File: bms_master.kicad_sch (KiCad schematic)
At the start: 94 parts, among them J1 Conn_01x02, J2 Conn_01x02, J3 Conn_01x02, J4 Conn_01x04, J5 Conn_01x04, J6 Conn_01x06, Q1 PMV15ENE, Q2 PMV74EPE, Q3 PMV74EPE, SW1 SW_Push, U1 TPS25961, U10 MAX6126, U2 TPS7B88, U3 MCP1700x-330xxMB, U4 STM32F103C8Tx, U5 TPS3851, U6 SN65HVD1050D, U7 M24C64-R, U8 741G3157, U9 MAX11163, Y1 8M

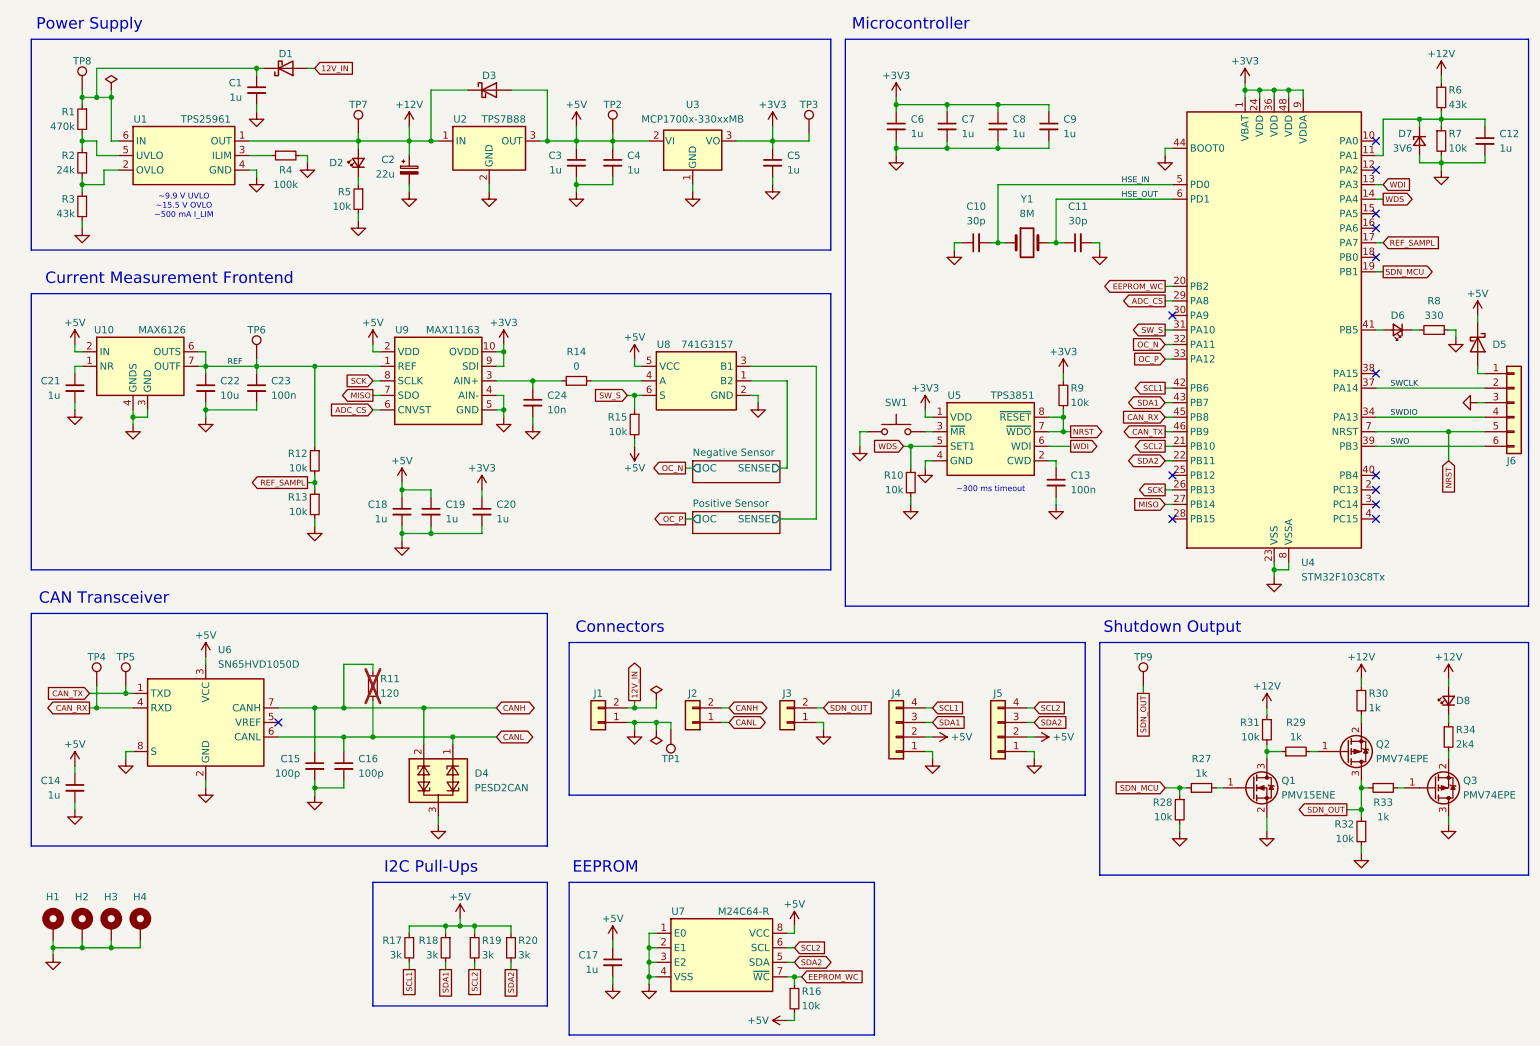
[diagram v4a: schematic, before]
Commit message: *: Switch from the TPS25961 eFuse to the TPS26625
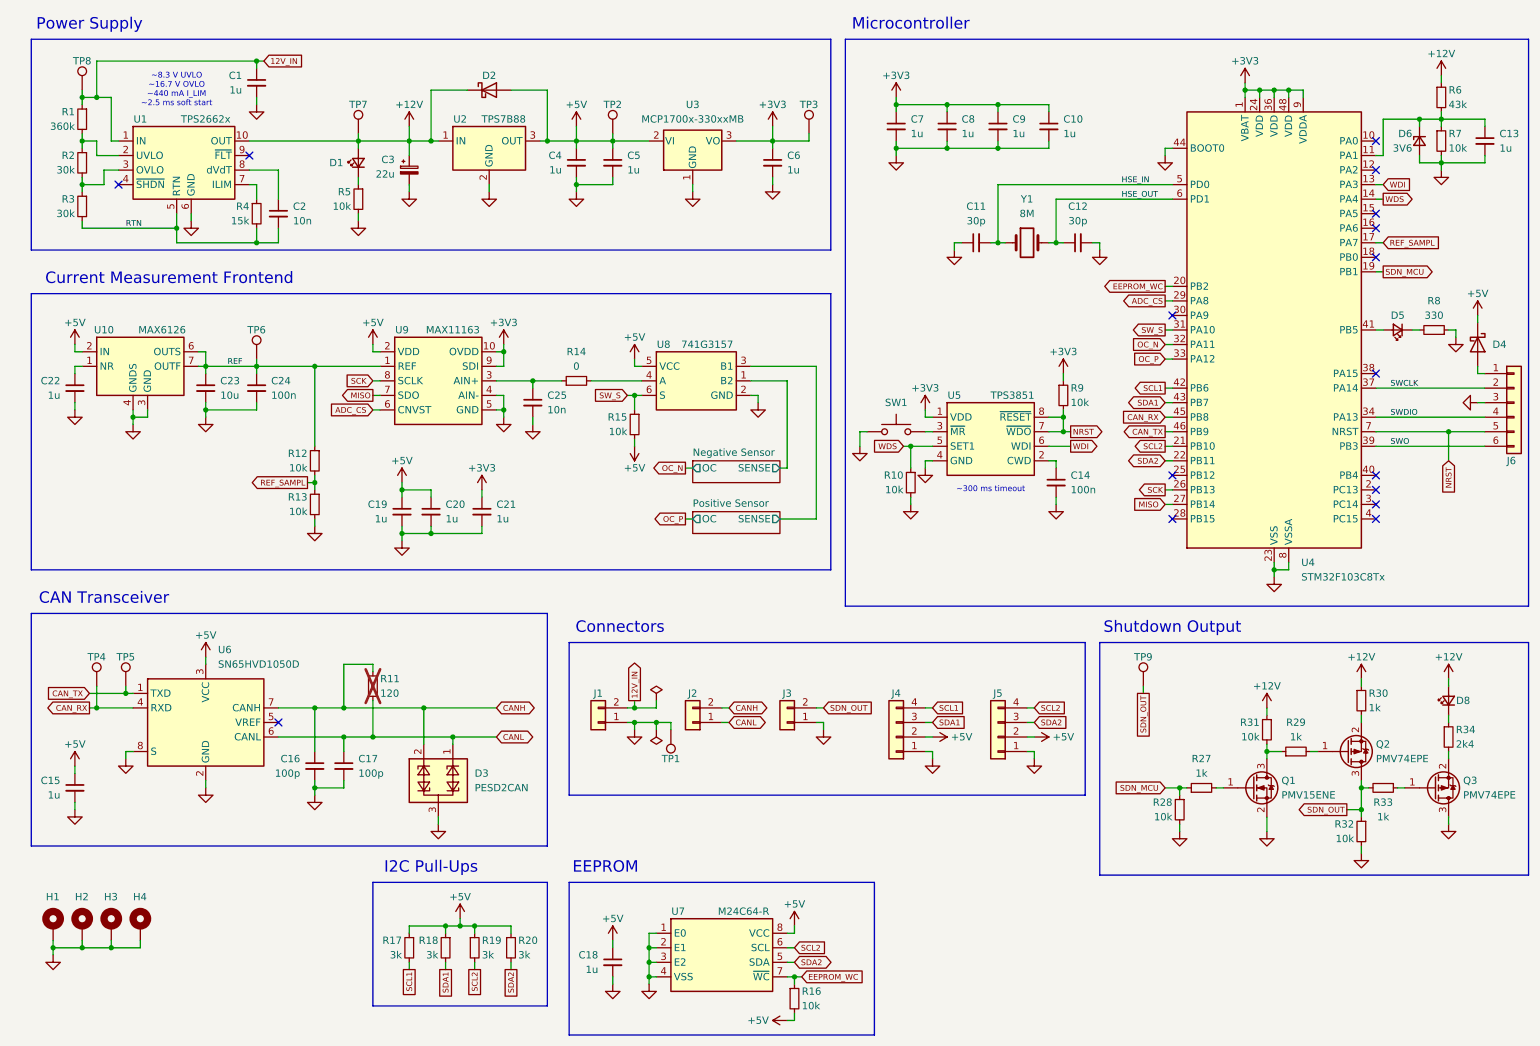
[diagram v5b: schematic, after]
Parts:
- removed D1: D_Schottky, Diode_SMD:D_SOD-323, symbol Device:D_Schottky
- removed U1: TPS25961, Package_SON:WSON-6-1EP_2x2mm_P0.65mm_EP1x1.6mm, symbol yfs:TPS25961
- added C2: 10n, Capacitor_SMD:C_0603_1608Metric, symbol Device:C_Small
- added U1: TPS2662x, Package_SON:VSON-10-1EP_3x3mm_P0.5mm_EP1.65x2.4mm, symbol yfs:TPS2662x
- R1: value 470k -> 360k
- R2: value 24k -> 30k
- R3: value 43k -> 30k
- R4: value 100k -> 15k
- renumbered C9 to C10, C10 to C11, C11 to C12, C12 to C13, C13 to C14, C14 to C15, C15 to C16, C16 to C17, C17 to C18, C18 to C19, C19 to C20, C20 to C21, C21 to C22, C22 to C23, C23 to C24, C24 to C25, C2 to C3, C3 to C4, C4 to C5, C5 to C6, C6 to C7, C7 to C8, C8 to C9, D2 to D1, D3 to D2, D4 to D3, D5 to D4, D6 to D5, D7 to D6
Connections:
- net +12V: now also U1.10 (OUT)
- net 12V_IN: now also C1.1, R1.1, TP8.1, U1.1 (IN)
- net GND: now also U1.6 (GND); no longer R3.2, R4.2
- net at R1.2, R2.1: now also U1.2 (UVLO)
- net at R2.2, R3.1: now also U1.3 (OVLO)
- net at R4.1: now also U1.7 (ILIM)
- new net: C2.1, U1.8 (dVdT)
- new net RTN: C2.2, R3.2, R4.2, U1.11 (RTN), U1.5 (RTN)
- no-connect marks 14 -> 16
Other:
- note added: "~8.3 V UVLO ~16.7 V OVLO ~440 mA I_LIM ~2.5 ms soft start"
- note removed: "~9.9 V UVLO ~15.5 V OVLO ~500 mA I_LIM"
- moved on the sheet: C1

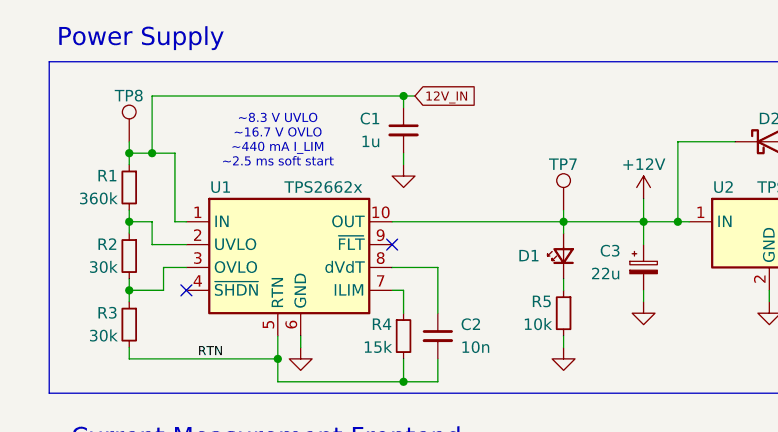
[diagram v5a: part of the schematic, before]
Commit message: *: Add a TVS diode on the LVS input
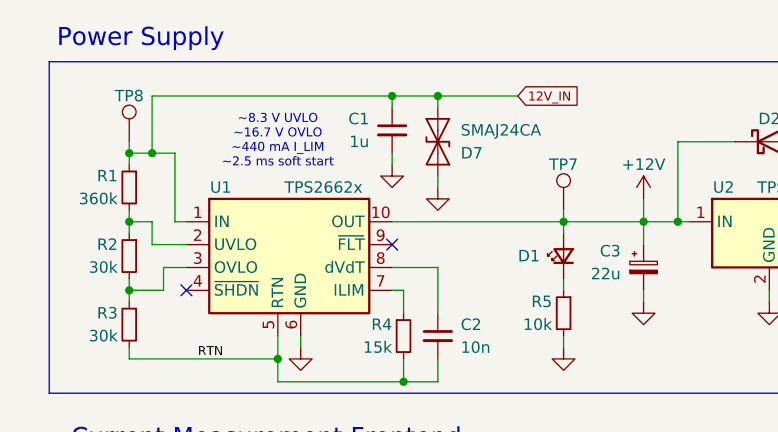
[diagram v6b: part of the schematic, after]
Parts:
- added D7: SMAJ24CA, Diode_SMD:D_SMA, symbol Diode:SMAJ24CA
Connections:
- net 12V_IN: now also D7.2 (A2)
- net GND: now also D7.1 (A1)
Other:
- moved on the sheet: C1
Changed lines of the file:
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@@
 	)
 	(junction
+		(at 58.42 21.59)
+		(diameter 0)
+		(color 0 0 0 0)
+	)
+	(junction
 		(at 128.27 176.53)
 		(diameter 0)
@@
 	)
 	(junction
+		(at 63.5 21.59)
+		(diameter 0)
+		(color 0 0 0 0)
+	)
+	(junction
 		(at 237.49 110.49)
 		(diameter 0)
@@
 	)
 	(junction
-		(at 59.69 21.59)
-		(diameter 0)
-		(color 0 0 0 0)
-	)
-	(junction
 		(at 220.98 148.59)
 		(diameter 0)
@@
 	(wire
 		(pts
-			(xy 59.69 29.21) (xy 59.69 27.94)
+			(xy 58.42 29.21) (xy 58.42 27.94)
 		)
 		(stroke
@@
 	(wire
 		(pts
+			(xy 63.5 21.59) (xy 72.39 21.59)
+		)
+		(stroke
+			(width 0)
+			(type default)
+		)
+	)
+	(wire
+		(pts
 			(xy 267.97 86.36) (xy 274.32 86.36)
 		)
@@
 	(wire
 		(pts
-			(xy 60.96 21.59) (xy 59.69 21.59)
-		)
-		(stroke
-			(width 0)
-			(type default)
-		)
-	)
-	(wire
-		(pts
 			(xy 262.89 38.1) (xy 262.89 39.37)
 		)
@@
 	(wire
 		(pts
+			(xy 63.5 30.48) (xy 63.5 31.75)
+		)
+		(stroke
+			(width 0)
+			(type default)
+		)
+	)
+	(wire
+		(pts
 			(xy 31.75 134.62) (xy 38.1 134.62)
 		)
@@
 	(wire
 		(pts
-			(xy 31.75 21.59) (xy 59.69 21.59)
+			(xy 31.75 21.59) (xy 58.42 21.59)
 		)
 		(stroke
@@
 	(wire
 		(pts
+			(xy 63.5 21.59) (xy 63.5 22.86)
+		)
+		(stroke
+			(width 0)
+			(type default)
+		)
+	)
+	(wire
+		(pts
 			(xy 102.87 82.55) (xy 102.87 83.82)
 		)
@@
 	(wire
 		(pts
-			(xy 59.69 21.59) (xy 59.69 22.86)
+			(xy 58.42 21.59) (xy 58.42 22.86)
 		)
 		(stroke
@@
 	(wire
 		(pts
+			(xy 58.42 21.59) (xy 63.5 21.59)
+		)
+		(stroke
+			(width 0)
+			(type default)
+		)
+	)
+	(wire
+		(pts
 			(xy 252.73 152.4) (xy 252.73 153.67)
 		)
@@
 	(global_label "12V_IN"
 		(shape input)
-		(at 60.96 21.59 0)
+		(at 72.39 21.59 0)
 		(fields_autoplaced yes)
 		(effects
@@
 		)
 		(property "Intersheetrefs" "${INTERSHEET_REFS}"
-			(at 68.3579 21.59 0)
+			(at 79.7879 21.59 0)
 			(effects
 				(font
@@
 	)
 	(symbol
+		(lib_id "power:GND")
+		(at 63.5 31.75 0)
+		(unit 1)
+		(exclude_from_sim no)
+		(in_bom yes)
+		(on_board yes)
+		(dnp no)
+		(fields_autoplaced yes)
+		(property "Reference" "#PWR047"
+			(at 63.5 38.1 0)
+			(effects
+				(font
+					(size 1.27 1.27)
+				)
+				(hide yes)
+			)
+		)
+		(property "Value" "GND"
+			(at 63.5 36.83 0)
+			(effects
+				(font
+					(size 1.27 1.27)
+				)
+				(hide yes)
+			)
+		)
+		(property "Footprint" ""
+			(at 63.5 31.75 0)
+			(effects
+				(font
+					(size 1.27 1.27)
+				)
+				(hide yes)
+			)
+		)
+		(property "Datasheet" ""
+			(at 63.5 31.75 0)
+			(effects
+				(font
+					(size 1.27 1.27)
+				)
+				(hide yes)
+			)
+		)
+		(property "Description" "Power symbol creates a global label with name \"GND\" , ground"
+			(at 63.5 31.75 0)
+			(effects
+				(font
+					(size 1.27 1.27)
+				)
+				(hide yes)
+			)
+		)
+		(pin "1"
+		)
+		(instances
+			(project "bms_master"
+				(path "/ff788b45-a486-492a-a3f3-4e15ca08a026"
+					(reference "#PWR047")
+					(unit 1)
+				)
+			)
+		)
+	)
+	(symbol
 		(lib_id "power:+5V")
 		(at 125.73 73.66 0)
@@
 	)
 	(symbol
+		(lib_id "Diode:SMAJ24CA")
+		(at 63.5 26.67 90)
+		(unit 1)
+		(exclude_from_sim no)
+		(in_bom yes)
+		(on_board yes)
+		(dnp no)
+		(property "Reference" "D7"
+			(at 66.04 27.94 90)
+			(effects
+				(font
+					(size 1.27 1.27)
+				)
+				(justify right)
+			)
+		)
+		(property "Value" "SMAJ24CA"
+			(at 66.04 25.4 90)
+			(effects
+				(font
+					(size 1.27 1.27)
+				)
+				(justify right)
+			)
+		)
+		(property "Footprint" "Diode_SMD:D_SMA"
+			(at 68.58 26.67 0)
+			(effects
+				(font
+					(size 1.27 1.27)
+				)
+				(hide yes)
+			)
+		)
+		(property "Datasheet" "https://www.littelfuse.com/media?resourcetype=datasheets&itemid=75e32973-b177-4ee3-a0ff-cedaf1abdb93&filename=smaj-datasheet"
+			(at 63.5 26.67 0)
+			(effects
+				(font
+					(size 1.27 1.27)
+				)
+				(hide yes)
+			)
+		)
+		(property "Description" "400W bidirectional Transient Voltage Suppressor, 24.0Vr, SMA(DO-214AC)"
+			(at 63.5 26.67 0)
+			(effects
+				(font
+					(size 1.27 1.27)
+				)
+				(hide yes)
+			)
+		)
+		(pin "2"
+		)
+		(pin "1"
+		)
+		(instances
+			(project ""
+				(path "/ff788b45-a486-492a-a3f3-4e15ca08a026"
+					(reference "D7")
+					(unit 1)
+				)
+			)
+		)
+	)
+	(symbol
 		(lib_id "power:GND")
 		(at 69.85 149.86 0)
@@
 	(symbol
 		(lib_id "power:GND")
-		(at 59.69 29.21 0)
+		(at 58.42 29.21 0)
 		(unit 1)
 		(exclude_from_sim no)
@@
 		(fields_autoplaced yes)
 		(property "Reference" "#PWR045"
-			(at 59.69 35.56 0)
+			(at 58.42 35.56 0)
 			(effects
 				(font
@@
 		)
 		(property "Value" "GND"
-			(at 59.69 34.29 0)
+			(at 58.42 34.29 0)
 			(effects
 				(font
@@
 		)
 		(property "Footprint" ""
-			(at 59.69 29.21 0)
+			(at 58.42 29.21 0)
 			(effects
 				(font
@@
 		)
 		(property "Datasheet" ""
-			(at 59.69 29.21 0)
+			(at 58.42 29.21 0)
 			(effects
 				(font
@@
 		)
 		(property "Description" "Power symbol creates a global label with name \"GND\" , ground"
-			(at 59.69 29.21 0)
+			(at 58.42 29.21 0)
 			(effects
 				(font
@@
 	(symbol
 		(lib_id "Device:C_Small")
-		(at 59.69 25.4 0)
+		(at 58.42 25.4 0)
 		(mirror y)
 		(unit 1)
@@
 		(dnp no)
 		(property "Reference" "C1"
-			(at 57.15 24.1362 0)
+			(at 55.88 24.1362 0)
 			(effects
 				(font
@@
 		)
 		(property "Value" "1u"
-			(at 57.15 26.6762 0)
+			(at 55.88 26.6762 0)
 			(effects
 				(font
@@
 		)
 		(property "Footprint" "Capacitor_SMD:C_0603_1608Metric"
-			(at 59.69 25.4 0)
+			(at 58.42 25.4 0)
 			(effects
 				(font
@@
 		)
 		(property "Datasheet" "~"
-			(at 59.69 25.4 0)
+			(at 58.42 25.4 0)
 			(effects
 				(font
@@
 		)
 		(property "Description" "Unpolarized capacitor, small symbol"
-			(at 59.69 25.4 0)
+			(at 58.42 25.4 0)
 			(effects
 				(font
@@
 		)
 		(property "Dist #" "C5199872"
-			(at 59.69 25.4 0)
+			(at 58.42 25.4 0)
 			(effects
 				(font
@@
 		)
 		(property "Mfr" "Samsung"
-			(at 59.69 25.4 0)
+			(at 58.42 25.4 0)
 			(effects
 				(font
@@
 		)
 		(property "Mfr #" "CL10B105KB8NQNC"
-			(at 59.69 25.4 0)
+			(at 58.42 25.4 0)
 			(effects
 				(font
@@
 		)
 		(property "Dist" "LCSC"
-			(at 59.69 25.4 0)
+			(at 58.42 25.4 0)
 			(effects
 				(font
